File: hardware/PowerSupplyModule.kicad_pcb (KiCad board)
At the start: 4 copper layers, 85 x 170 mm, 277 parts, among them J1 Conn_01x02_Socket, J2 Conn_01x02_Socket, J3 Conn_01x08_Pin, J4 Conn_ARM_SWD_TagConnect_TC203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, K1 AZ576-1C-24DE, K2 AZ576-1A-24DE, K3 AZ576-1A-24DE, K4 AZ576-1A-24DE, Q1 IPZ40N04S5L4R8ATMA1, Q2 IPZ40N04S5L4R8ATMA1, Q3 IPZ40N04S5L4R8ATMA1, Q4 SISS76LDN-T1-GE3, SW1 1825910-6, U1 TPS55288, U10 LV2862XDDC, U11 LT3081EDF-TRPBF, U12 LT3081EDF-TRPBF, U13 LT3092xTS8, U14 AD5293, U15 MCP45HV51-ST, U16 AT24CS08-SSHM, U17 STM32C031K4Tx, U18 SN74LVC1G08, U19 TPL7407LPWR, U2 LT3081EDF-TRPBF, U20 SN74LVC1G08, U21 MIC826, U22 ISO1540, U23 SI8652EB-B-IU, U3 LT3081EDF-TRPBF, U4 TPS552872RYQR, U5 LT3081EDF-TRPBF, U6 LT3081EDF-TRPBF, U7 LT3081EDF-TRPBF, U8 TPS7A4701xRGW, U9 TPS7A4701xRGW

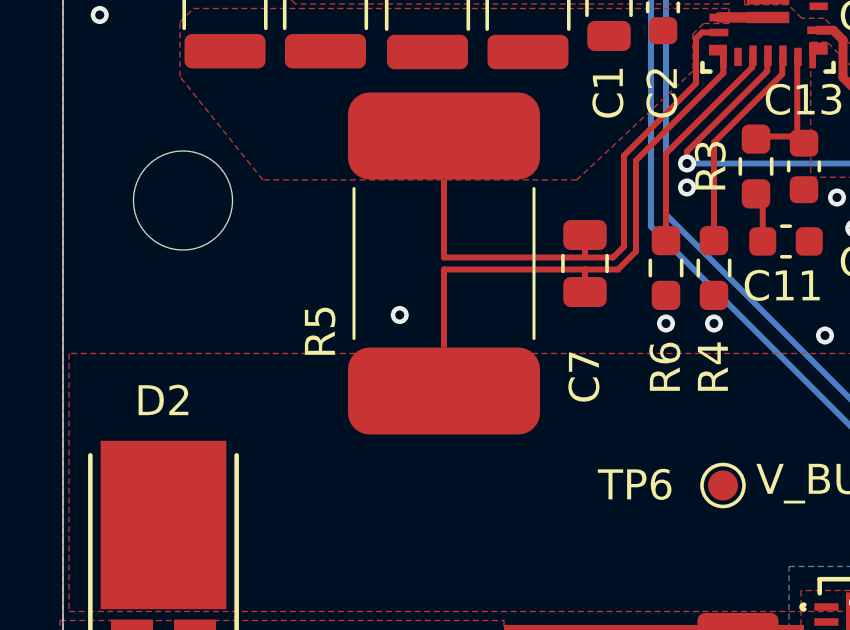
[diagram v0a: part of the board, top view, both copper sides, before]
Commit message: fixed kicad project errors
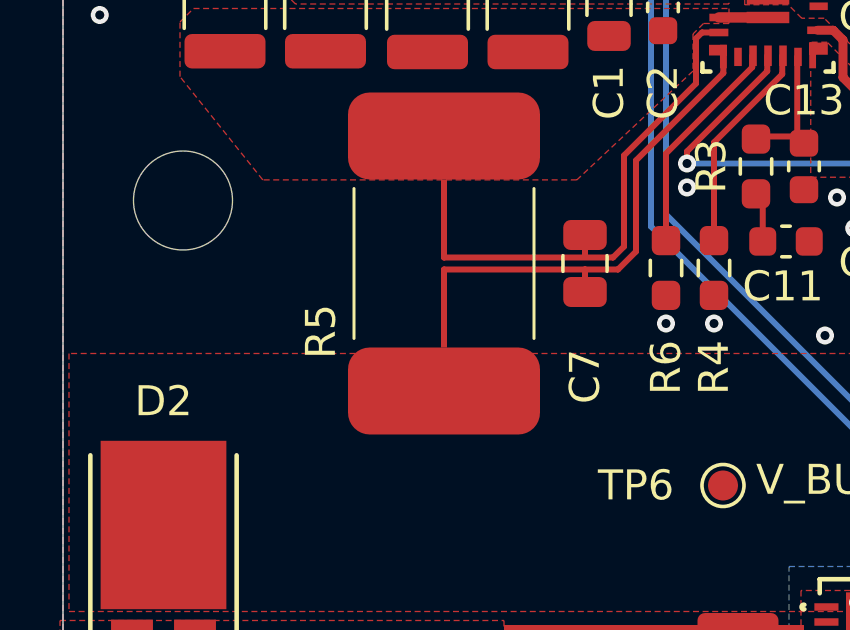
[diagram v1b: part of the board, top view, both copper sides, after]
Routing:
- net /GND: vias 504 -> 559
- net (no net): vias 91 -> 35
